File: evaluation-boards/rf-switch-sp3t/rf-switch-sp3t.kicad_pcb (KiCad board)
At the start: 4 copper layers, 100 x 25 mm, 33 parts, among them J1 Conn_Coaxial, J10 Conn_Coaxial, J11 Conn_Coaxial, J12 Conn_Coaxial, J13 Conn_01x02, J14 Conn_01x02, J15 Conn_02x06_Odd_Even, J2 Conn_Coaxial, J3 Conn_Coaxial, J4 Conn_Coaxial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

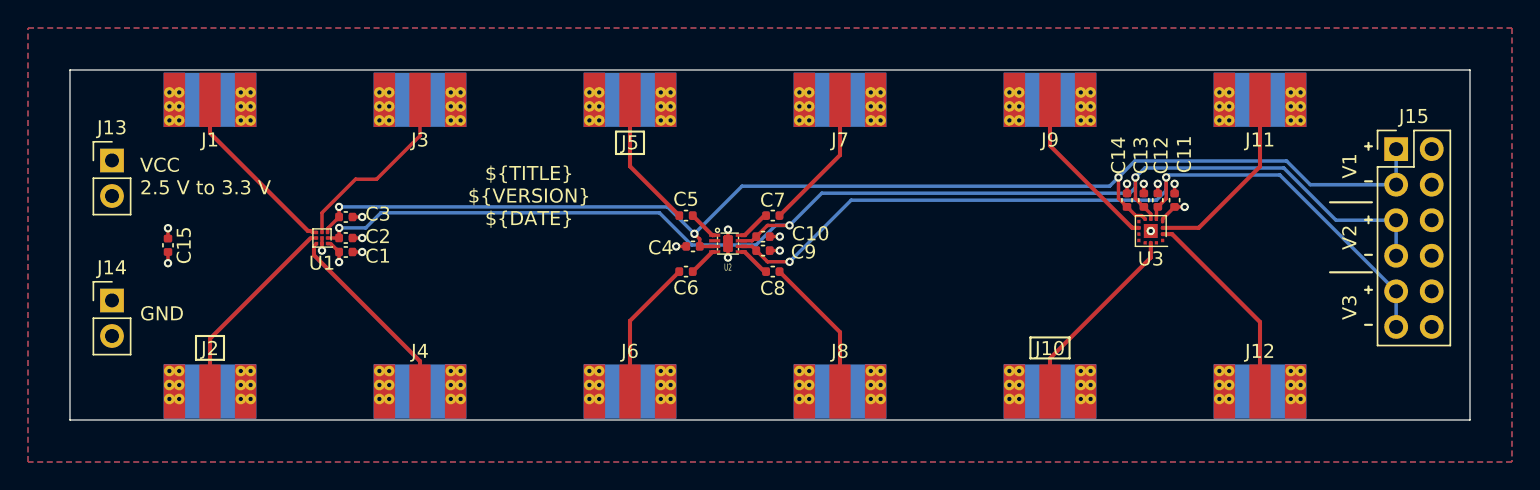
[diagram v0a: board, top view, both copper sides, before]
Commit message: Update RF test boards
- limiters
- rf-switch-spdt
- rf-switch-sp3t
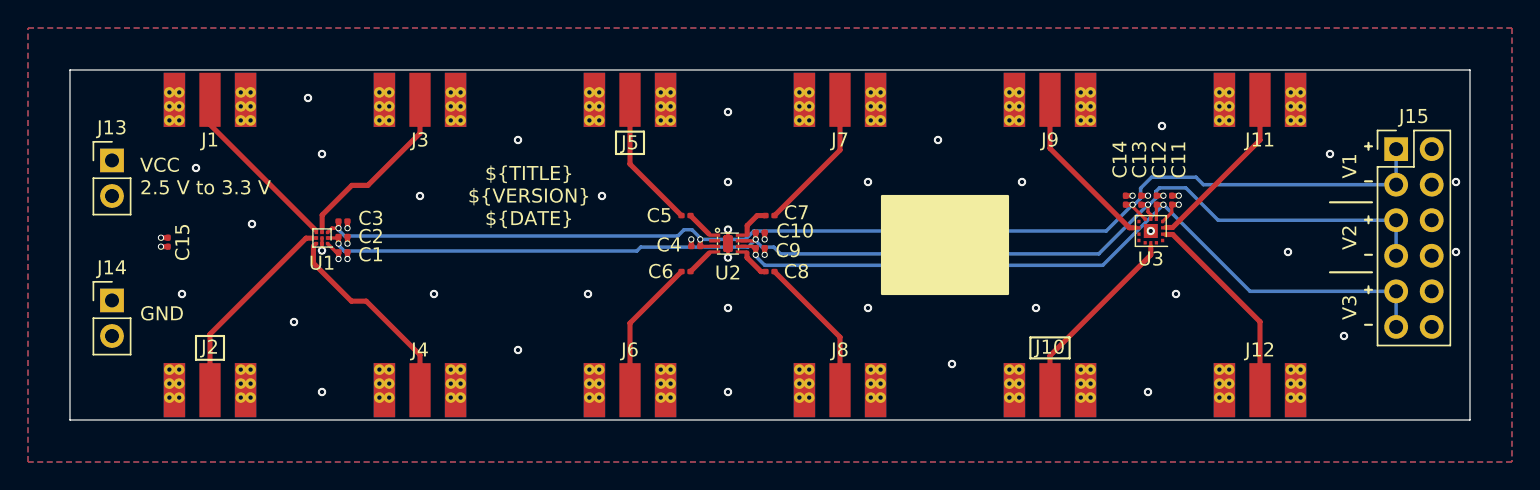
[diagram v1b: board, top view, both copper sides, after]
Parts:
- C1, C10, C11, C12, C13, C14, C15, C2, C3, C4, C5, C6, C7, C8, C9: footprint Capacitor_SMD:C_0402_1005Metric -> Capacitor_SMD:C_0201_0603Metric
- J1, J10, J11, J12, J2, J3, J4, J5, J6, J7, J8, J9: footprint eval:CONSMA003.062 -> sma-variants:Linx_SMA_CONSMA003.062
- moved C10 0.36 mm to (149.3, 106.6)
- moved C3 0.36 mm to (119.5, 105.8)
- moved C9 0.28 mm to (149.3, 107.7)
- moved C2 0.22 mm to (119.5, 106.9)
- moved C15 0.22 mm to (107.0, 107.3)
- moved C11 0.20 mm to (178.7, 104.3)
- moved C1 0.20 mm to (119.5, 108.0)
- moved C13 0.20 mm to (176.5, 104.3)
- moved C4 0.20 mm to (144.7, 107.6)
- moved C7 0.20 mm to (150.0, 105.4)
- moved C8 0.20 mm to (150.0, 109.4)
- moved C12 0.10 mm to (177.6, 104.3)
- moved C14 0.10 mm to (175.4, 104.3)
- moved J10 0.10 mm to (170.0, 120.0)
- moved J12 0.10 mm to (185.0, 120.0)
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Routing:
- net /V2: track 92.6 -> 86.9 mm
- net /V1: track 90.0 -> 86.2 mm
- net /V3: track 59.6 -> 56.1 mm
- net GND: track 10.7 -> 8.40 mm, vias 15 -> 46
- net Net-(J11-In): track 13.5 -> 12.2 mm
- net Net-(J4-In): track 13.8 -> 14.5 mm
- net VCC: track 4.65 -> 4.00 mm
- added copper zone on B.Cu, net GND
- added copper zone on F.Cu, net GND
- removed copper zone on B.Cu, net (none)
- removed copper zone on F.Cu, net (none)
